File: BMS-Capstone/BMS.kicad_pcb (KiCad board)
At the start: 2 copper layers, 92.7 x 127 mm, 50 parts, among them IC1 BQ7694204PFBR, J1 Conn_01x02_Socket, J2 Conn_01x02_Socket, J3 Conn_01x13_Socket, K1 J107F1CS203VDC.80, U1 Teensy4.0

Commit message: Appended the BMS board pcb
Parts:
- added C1: C, Capacitor_SMD:C_0805_2012Metric, F.Cu at (59.5, 57.6)
- added C10: C, Capacitor_SMD:C_0805_2012Metric, F.Cu at (56.0, 69.3)
- added C11: C, Capacitor_SMD:C_0805_2012Metric, F.Cu at (62.0, 96.3)
- added C12: C, Capacitor_SMD:C_0805_2012Metric, F.Cu at (52.7, 96.6)
- added C13: C, Capacitor_SMD:C_0805_2012Metric, F.Cu at (59.1, 99.5)
- added C14: C, Capacitor_SMD:C_0805_2012Metric, F.Cu at (53.5, 100.1)
- added C15: C, Capacitor_SMD:C_0805_2012Metric, F.Cu at (56.0, 90.7)
- added C16: C, Capacitor_SMD:C_0805_2012Metric, F.Cu at (89.7, 95.4)
- added C17: C, Capacitor_SMD:C_0805_2012Metric, F.Cu at (80.4, 95.7)
- added C18: C, Capacitor_SMD:C_0805_2012Metric, F.Cu at (86.9, 98.5)
- added C19: C, Capacitor_SMD:C_0805_2012Metric, F.Cu at (81.2, 99.1)
- added C2: C, Capacitor_SMD:C_0805_2012Metric, F.Cu at (53.9, 58.2)
- added C20: C, Capacitor_SMD:C_0805_2012Metric, F.Cu at (83.8, 89.7)
- added C21: C, Capacitor_SMD:C_0805_2012Metric, F.Cu at (89.4, 74.8)
- added C22: C, Capacitor_SMD:C_0805_2012Metric, F.Cu at (80.1, 75.1)
- added C23: C, Capacitor_SMD:C_0805_2012Metric, F.Cu at (86.5, 77.9)
- added C24: C, Capacitor_SMD:C_0805_2012Metric, F.Cu at (80.9, 78.5)
- added C25: C, Capacitor_SMD:C_0805_2012Metric, F.Cu at (83.4, 69.1)
- added C26: C, Capacitor_SMD:C_0805_2012Metric, F.Cu at (89.9, 54.6)
- added C27: C, Capacitor_SMD:C_0805_2012Metric, F.Cu at (80.6, 54.9)
- added C28: C, Capacitor_SMD:C_0805_2012Metric, F.Cu at (87.0, 57.8)
- added C29: C, Capacitor_SMD:C_0805_2012Metric, F.Cu at (81.4, 58.4)
- added C3: C, Capacitor_SMD:C_0805_2012Metric, F.Cu at (62.4, 54.5)
- added C30: C, Capacitor_SMD:C_0805_2012Metric, F.Cu at (83.9, 49.0)
- added C4: C, Capacitor_SMD:C_0805_2012Metric, F.Cu at (53.1, 54.8)
- added C5: C, Capacitor_SMD:C_0805_2012Metric, F.Cu at (56.5, 48.8)
- added C6: C, Capacitor_SMD:C_0805_2012Metric, F.Cu at (61.9, 75.0)
- added C7: C, Capacitor_SMD:C_0805_2012Metric, F.Cu at (52.6, 75.2)
- added C8: C, Capacitor_SMD:C_0805_2012Metric, F.Cu at (59.0, 78.1)
- added C9: C, Capacitor_SMD:C_0805_2012Metric, F.Cu at (53.4, 78.7)
- added IC1: MP2643, SamacSys_Parts:MP2639AGRZ, F.Cu at (58.0, 53.2)
- added IC2: MP2643, SamacSys_Parts:MP2639AGRZ, F.Cu at (57.5, 73.7)
- added IC3: MP2643, SamacSys_Parts:MP2639AGRZ, F.Cu at (57.6, 95.1)
- added IC4: MP2643, SamacSys_Parts:MP2639AGRZ, F.Cu at (85.3, 94.1)
- added IC5: MP2643, SamacSys_Parts:MP2639AGRZ, F.Cu at (85.0, 73.5)
- added IC6: MP2643, SamacSys_Parts:MP2639AGRZ, F.Cu at (85.5, 53.4)
- added J: Conn_01x13_Socket, Connector_PinHeader_2.54mm:PinHeader_1x13_P2.54mm_Vertical, F.Cu at (27.3, 90.2)
- added L1: L, SamacSys_Parts:MPLAL4020R47 Inductor, F.Cu at (51.5, 49.9)
- added L2: L, SamacSys_Parts:MPLAL4020R47 Inductor, F.Cu at (51.0, 70.4)
- added L3: L, SamacSys_Parts:MPLAL4020R47 Inductor, F.Cu at (51.1, 91.8)
- added L4: L, SamacSys_Parts:MPLAL4020R47 Inductor, F.Cu at (78.8, 90.8)
- added L5: L, SamacSys_Parts:MPLAL4020R47 Inductor, F.Cu at (78.5, 70.2)
- added L6: L, SamacSys_Parts:MPLAL4020R47 Inductor, F.Cu at (79.0, 50.1)
- added Q1: FODM121, SamacSys_Parts:SOP254P675X240-4N, F.Cu at (70.5, 54.6)
- added Q10: FODM121, SamacSys_Parts:SOP254P675X240-4N, F.Cu at (97.5, 79.6)
- added Q11: FODM121, SamacSys_Parts:SOP254P675X240-4N, F.Cu at (98.0, 54.8)
- added Q12: FODM121, SamacSys_Parts:SOP254P675X240-4N, F.Cu at (98.0, 59.5)
- added Q2: FODM121, SamacSys_Parts:SOP254P675X240-4N, F.Cu at (70.5, 59.3)
- added Q3: FODM121, SamacSys_Parts:SOP254P675X240-4N, F.Cu at (70.0, 75.1)
- added Q4: FODM121, SamacSys_Parts:SOP254P675X240-4N, F.Cu at (70.0, 79.8)
- added Q5: FODM121, SamacSys_Parts:SOP254P675X240-4N, F.Cu at (70.1, 96.5)
- added Q6: FODM121, SamacSys_Parts:SOP254P675X240-4N, F.Cu at (70.1, 101.2)
- added Q7: FODM121, SamacSys_Parts:SOP254P675X240-4N, F.Cu at (97.8, 95.5)
- added Q8: FODM121, SamacSys_Parts:SOP254P675X240-4N, F.Cu at (97.8, 100.2)
- added Q9: FODM121, SamacSys_Parts:SOP254P675X240-4N, F.Cu at (97.5, 74.9)
- added R1: R, Resistor_SMD:R_0805_2012Metric, F.Cu at (59.2, 48.1)
- added R10: 0, Resistor_SMD:R_0805_2012Metric, F.Cu at (60.6, 68.6)
- added R11: R, Resistor_SMD:R_0805_2012Metric, F.Cu at (58.7, 68.6)
- added R12: R, Resistor_SMD:R_0805_2012Metric, F.Cu at (55.4, 78.7)
- added R13: R, Resistor_SMD:R_0805_2012Metric, F.Cu at (58.2, 80.8)
- added R14: R, Resistor_SMD:R_0805_2012Metric, F.Cu at (60.1, 80.8)
- added R15: R, Resistor_SMD:R_0805_2012Metric, F.Cu at (64.0, 97.9)
- added R16: R, Resistor_SMD:R_0805_2012Metric, F.Cu at (64.0, 94.5)
- added R17: 0, Resistor_SMD:R_0805_2012Metric, F.Cu at (60.7, 90.0)
- added R18: R, Resistor_SMD:R_0805_2012Metric, F.Cu at (58.8, 90.0)
- added R19: R, Resistor_SMD:R_0805_2012Metric, F.Cu at (55.5, 100.1)
- added R2: R, Resistor_SMD:R_0805_2012Metric, F.Cu at (61.1, 48.1)
- added R20: R, Resistor_SMD:R_0805_2012Metric, F.Cu at (58.3, 102.2)
- added R21: R, Resistor_SMD:R_0805_2012Metric, F.Cu at (60.2, 102.2)
- added R22: R, Resistor_SMD:R_0805_2012Metric, F.Cu at (91.7, 96.9)
- added R23: R, Resistor_SMD:R_0805_2012Metric, F.Cu at (91.7, 93.5)
- added R24: 0, Resistor_SMD:R_0805_2012Metric, F.Cu at (88.4, 89.0)
- added R25: R, Resistor_SMD:R_0805_2012Metric, F.Cu at (86.5, 89.0)
- added R26: R, Resistor_SMD:R_0805_2012Metric, F.Cu at (83.2, 99.1)
- added R27: R, Resistor_SMD:R_0805_2012Metric, F.Cu at (86.0, 101.2)
- added R28: R, Resistor_SMD:R_0805_2012Metric, F.Cu at (87.9, 101.2)
- added R29: R, Resistor_SMD:R_0805_2012Metric, F.Cu at (91.4, 76.3)
- added R3: 0, Resistor_SMD:R_0805_2012Metric, F.Cu at (55.9, 58.2)
- added R30: R, Resistor_SMD:R_0805_2012Metric, F.Cu at (91.4, 72.9)
- added R31: 0, Resistor_SMD:R_0805_2012Metric, F.Cu at (88.1, 68.4)
- added R32: R, Resistor_SMD:R_0805_2012Metric, F.Cu at (86.2, 68.4)
- added R33: R, Resistor_SMD:R_0805_2012Metric, F.Cu at (82.9, 78.5)
- added R34: R, Resistor_SMD:R_0805_2012Metric, F.Cu at (85.7, 80.6)
- added R35: R, Resistor_SMD:R_0805_2012Metric, F.Cu at (87.6, 80.6)
- added R36: R, Resistor_SMD:R_0805_2012Metric, F.Cu at (91.9, 56.2)
- added R37: R, Resistor_SMD:R_0805_2012Metric, F.Cu at (91.9, 52.8)
- added R38: 0, Resistor_SMD:R_0805_2012Metric, F.Cu at (88.6, 48.3)
- added R39: R, Resistor_SMD:R_0805_2012Metric, F.Cu at (86.7, 48.3)
- added R4: R, Resistor_SMD:R_0805_2012Metric, F.Cu at (64.4, 56.0)
- added R40: R, Resistor_SMD:R_0805_2012Metric, F.Cu at (83.4, 58.4)
- added R41: R, Resistor_SMD:R_0805_2012Metric, F.Cu at (86.2, 60.5)
- added R42: R, Resistor_SMD:R_0805_2012Metric, F.Cu at (88.1, 60.5)
- added R5: R, Resistor_SMD:R_0805_2012Metric, F.Cu at (64.4, 52.6)
- added R6: R, Resistor_SMD:R_0805_2012Metric, F.Cu at (58.7, 60.3)
- added R7: R, Resistor_SMD:R_0805_2012Metric, F.Cu at (60.6, 60.3)
- added R8: R, Resistor_SMD:R_0805_2012Metric, F.Cu at (63.9, 76.5)
- added R9: R, Resistor_SMD:R_0805_2012Metric, F.Cu at (63.9, 73.1)
- moved C1 39.8 mm to (147.8, 69.2)
- moved C6 39.8 mm to (141.8, 64.7)
- moved C10 39.8 mm to (149.2, 53.7)
- moved C11 39.8 mm to (154.2, 57.2)
- moved C12 39.8 mm to (157.2, 60.2)
- moved C13 39.8 mm to (157.2, 62.7)
- moved C14 39.8 mm to (151.2, 70.7)
- moved C15 39.8 mm to (153.8, 73.1)
- moved C16 39.8 mm to (154.8, 66.9)
- moved C2 39.8 mm to (147.8, 75.2)
- moved C3 39.8 mm to (144.8, 73.2)
- moved C5 39.8 mm to (142.2, 67.2)
- moved C7 39.8 mm to (141.8, 61.6)
- moved C8 39.8 mm to (146.0, 54.9)
- moved C9 39.8 mm to (146.2, 52.3)
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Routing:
- net /BMS Board/1Upper: track 0.00 -> 47.8 mm, vias 0 -> 17
- net /BMS Board/2Upper: track 0.00 -> 47.8 mm, vias 0 -> 17
- net /BMS Board/4Upper: track 0.00 -> 47.8 mm, vias 0 -> 17
- net /BMS Board/3Upper: track 0.00 -> 47.8 mm, vias 0 -> 17
- net /BMS Board/5Upper: track 0.00 -> 41.3 mm, vias 0 -> 6
- net /BMS Board/1Lower: track 0.00 -> 30.3 mm, vias 0 -> 15
- net Net-(IC1-MODE): track 0.00 -> 20.0 mm
- net Net-(IC3-MODE): track 0.00 -> 20.0 mm
- net Net-(IC2-MODE): track 0.00 -> 20.0 mm
- net Net-(IC6-MODE): track 0.00 -> 20.0 mm
- net Net-(IC5-MODE): track 0.00 -> 20.0 mm
- net Net-(IC4-MODE): track 0.00 -> 20.0 mm
- net Net-(IC3-EN): track 0.00 -> 17.8 mm
- net Net-(IC5-EN): track 0.00 -> 17.8 mm
- net Net-(IC1-EN): track 0.00 -> 17.8 mm
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- added copper zone on B.Cu, net /BMS Board/1Lower

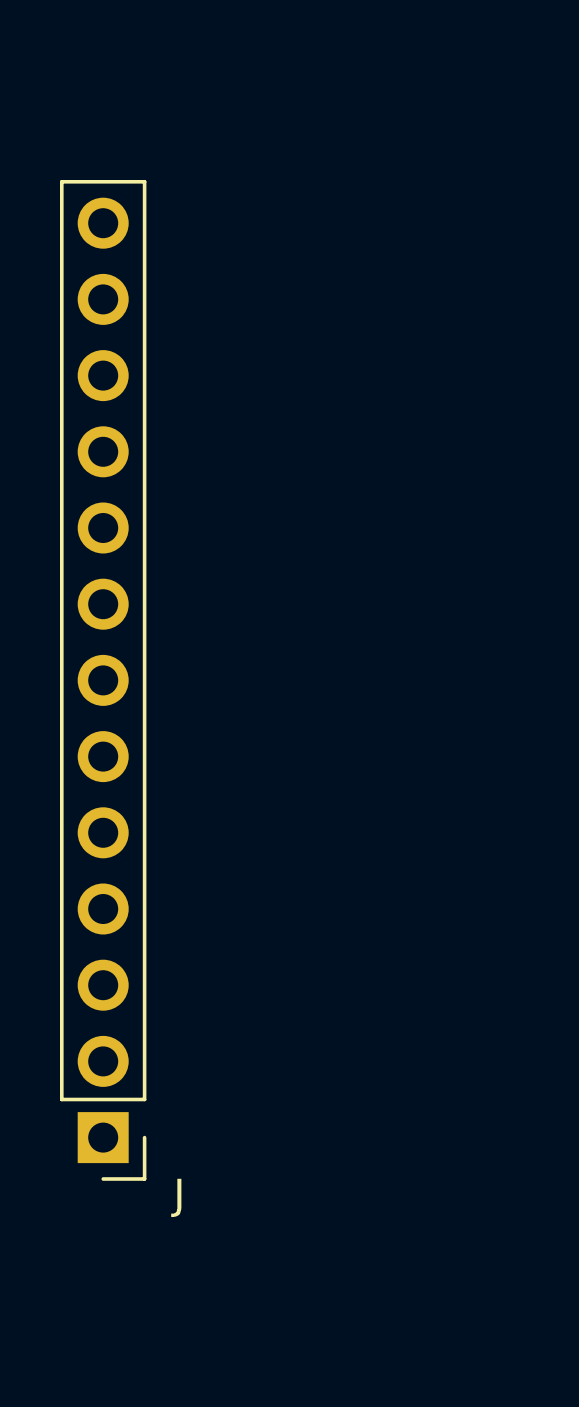
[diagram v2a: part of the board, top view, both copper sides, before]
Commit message: Added connector to balancing schematic
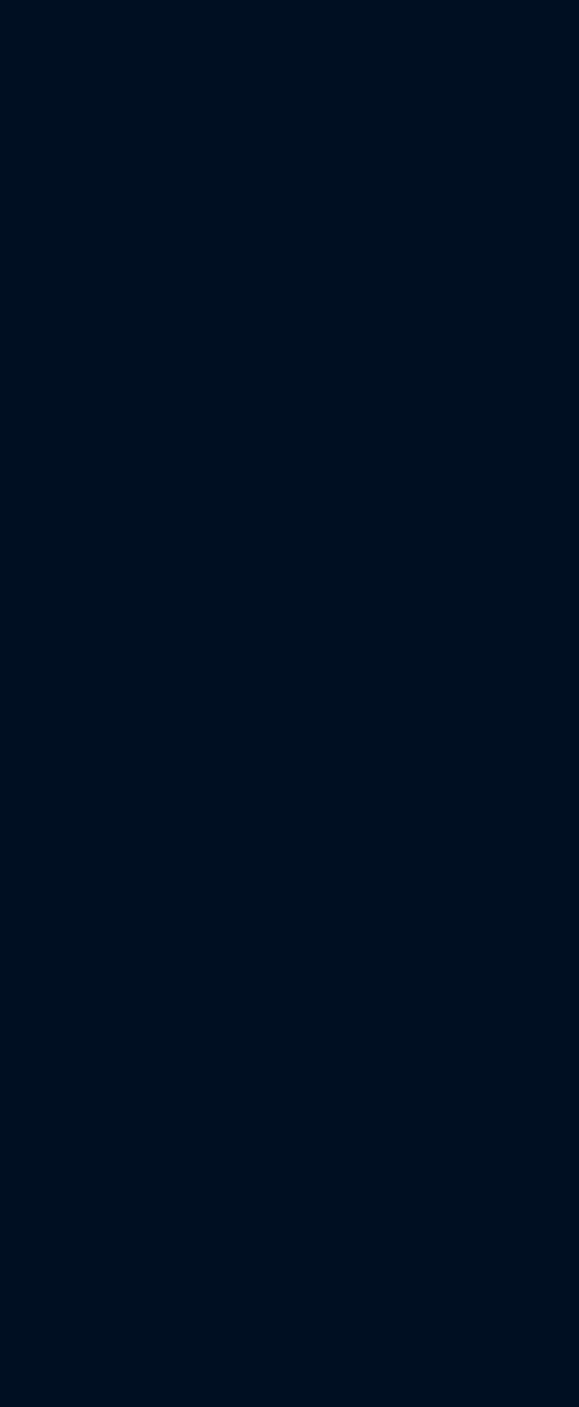
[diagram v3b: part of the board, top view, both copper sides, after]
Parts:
- removed J: Conn_01x13_Socket, Connector_PinHeader_2.54mm:PinHeader_1x13_P2.54mm_Vertical

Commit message: relinked footprints
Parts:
- added J: Conn_01x13_Socket, Connector_PinHeader_2.54mm:PinHeader_1x13_P2.54mm_Vertical, F.Cu at (27.3, 90.2)
